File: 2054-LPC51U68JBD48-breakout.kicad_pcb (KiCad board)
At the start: 2 copper layers, 62.2 x 19 mm, 24 parts, among them J1 Conn_01x24, J2 Conn_01x24, J4 10118194-0001LF, U1 LPC51U68JBD48, U2 AZ1117CH-3.3TRG1

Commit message: Reduce soldermask expansion to 1.8mil
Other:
- rule pad_to_mask_clearance: 0.0508 -> 0.04572
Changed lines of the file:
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@@
     (pad_size 1.524 1.524)
     (pad_drill 0.762)
-    (pad_to_mask_clearance 0.0508)
+    (pad_to_mask_clearance 0.04572)
     (solder_mask_min_width 0.1016)
     (aux_axis_origin 0 0)
@@
       (plotinvisibletext false)
       (padsonsilk false)
-      (subtractmaskfromsilk false)
+      (subtractmaskfromsilk true)
       (outputformat 1)
       (mirror false)

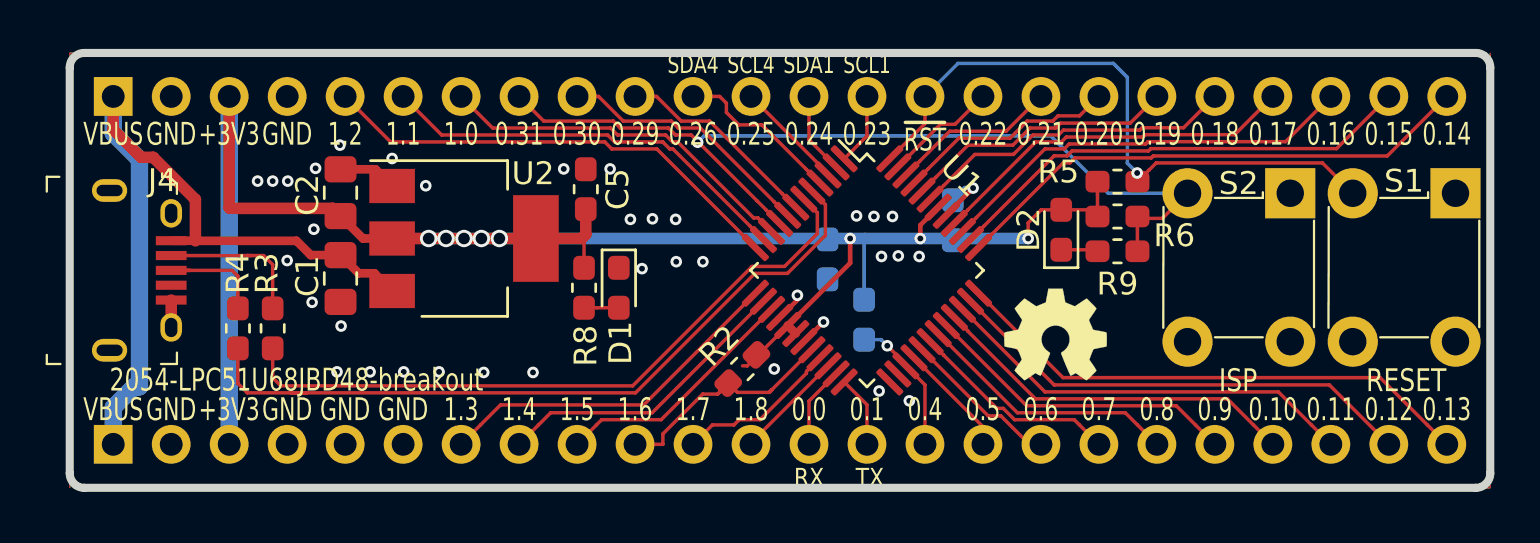
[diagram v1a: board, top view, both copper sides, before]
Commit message: CHanged Rev number on schematic & PCB.
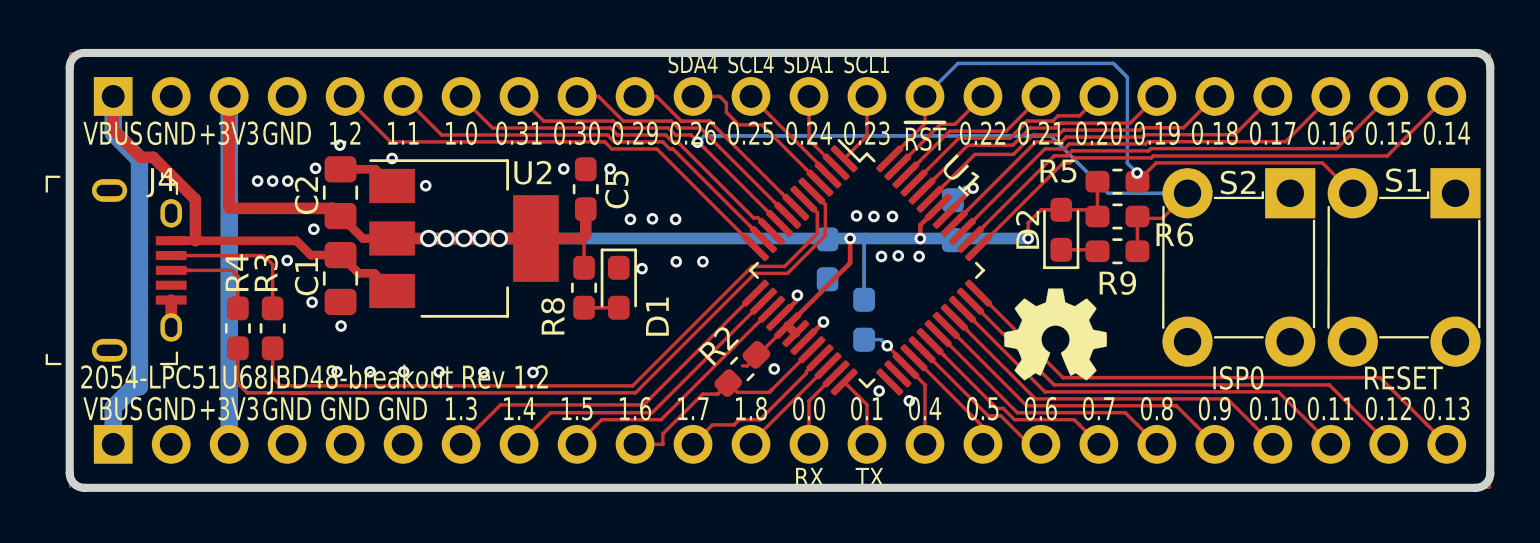
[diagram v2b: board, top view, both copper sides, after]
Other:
- board text added: "2054-LPC51U68JBD48-breakout Rev 1.2"
- board text added: "ISP0"
- board text removed: "2054-LPC51U68JBD48-breakout"
- board text removed: "ISP"
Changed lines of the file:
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@@
     (tags "LED handsolder")
     (attr smd)
-    (fp_text reference D1 (at 2.413 -0.0762 90) (layer F.SilkS)
+    (fp_text reference D1 (at 1.27 -1.7272 90) (layer F.SilkS)
       (effects (font (size 1 1) (thickness 0.15)))
     )
@@
     (tags "resistor handsolder")
     (attr smd)
-    (fp_text reference R8 (at -2.54 0.0762 90) (layer F.SilkS)
+    (fp_text reference R8 (at -1.27 -1.3208 90) (layer F.SilkS)
       (effects (font (size 1 1) (thickness 0.15)))
     )
@@
       (xy 0.555814 2.531069)) (layer B.SilkS) (width 0.01))
   )
-  (gr_text ISP (at 183.896 101.346) (layer F.SilkS)
+  (gr_text ISP0 (at 183.896 101.2698) (layer F.SilkS)
     (effects (font (size 1 0.8) (thickness 0.15)))
   )
-  (gr_text RESET (at 191.262 101.346) (layer F.SilkS)
+  (gr_text RESET (at 191.1096 101.2698) (layer F.SilkS)
     (effects (font (size 1 0.8) (thickness 0.15)))
   )
@@
     (effects (font (size 0.8 0.7) (thickness 0.15)))
   )
-  (gr_text 2054-LPC51U68JBD48-breakout (at 142.6464 101.3206) (layer F.SilkS)
-    (effects (font (size 1 0.75) (thickness 0.15)))
+  (gr_text "2054-LPC51U68JBD48-breakout Rev 1.2" (at 133.14426 101.22916) (layer F.SilkS)
+    (effects (font (size 1 0.75) (thickness 0.15)) (justify left))
   )
   (gr_arc (start 194.31 87.63) (end 194.945 87.63) (angle -90) (layer Edge.Cuts) (width 0.3556))
